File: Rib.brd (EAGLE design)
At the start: 127 x 87.6 mm, 34 parts, among them IC1 REG1117, IC2 REG1117

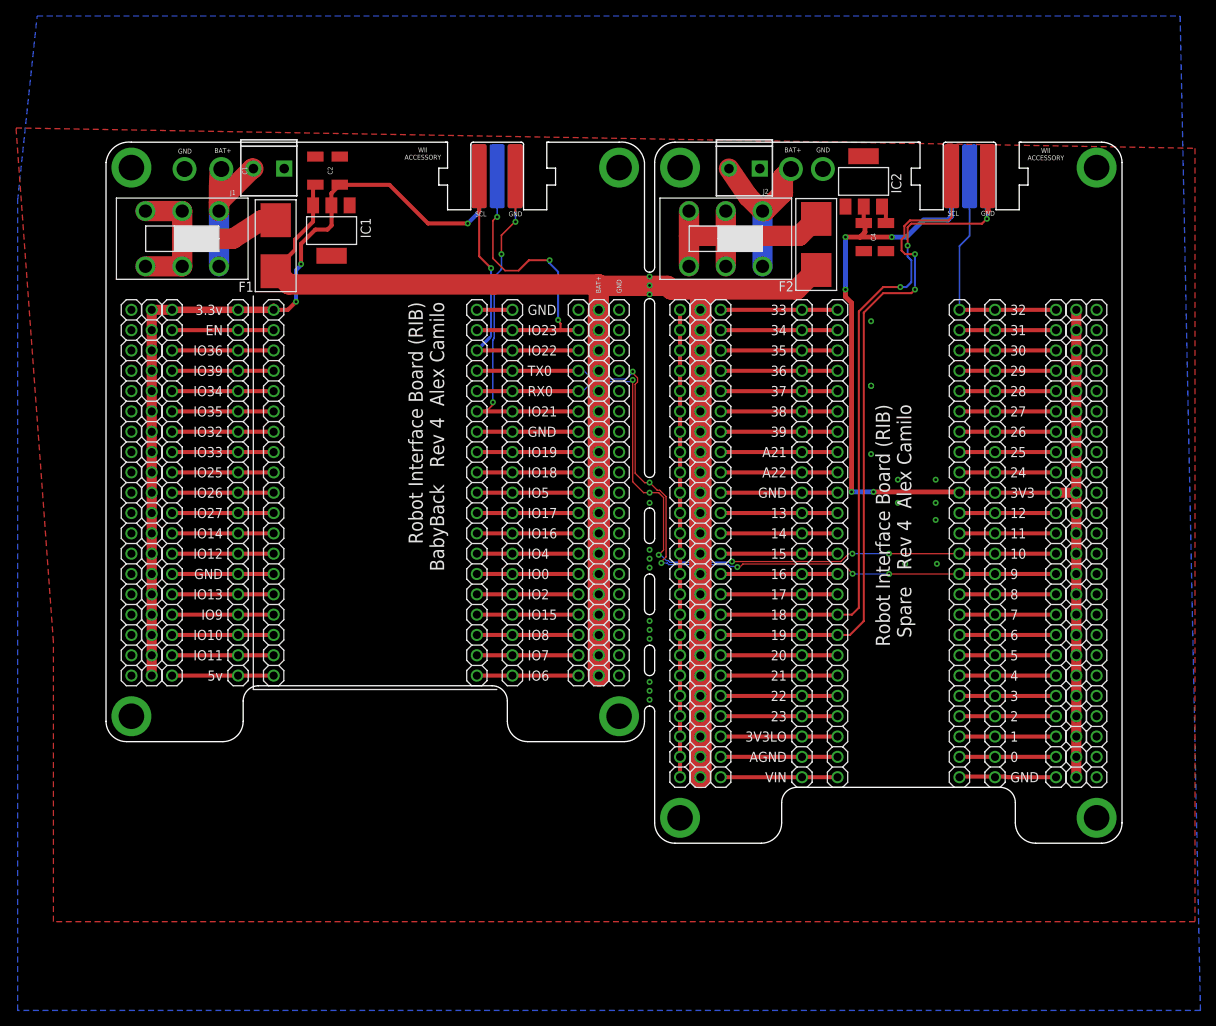
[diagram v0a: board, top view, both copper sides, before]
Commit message: Replaced fuseholder with blade style automotive fuse
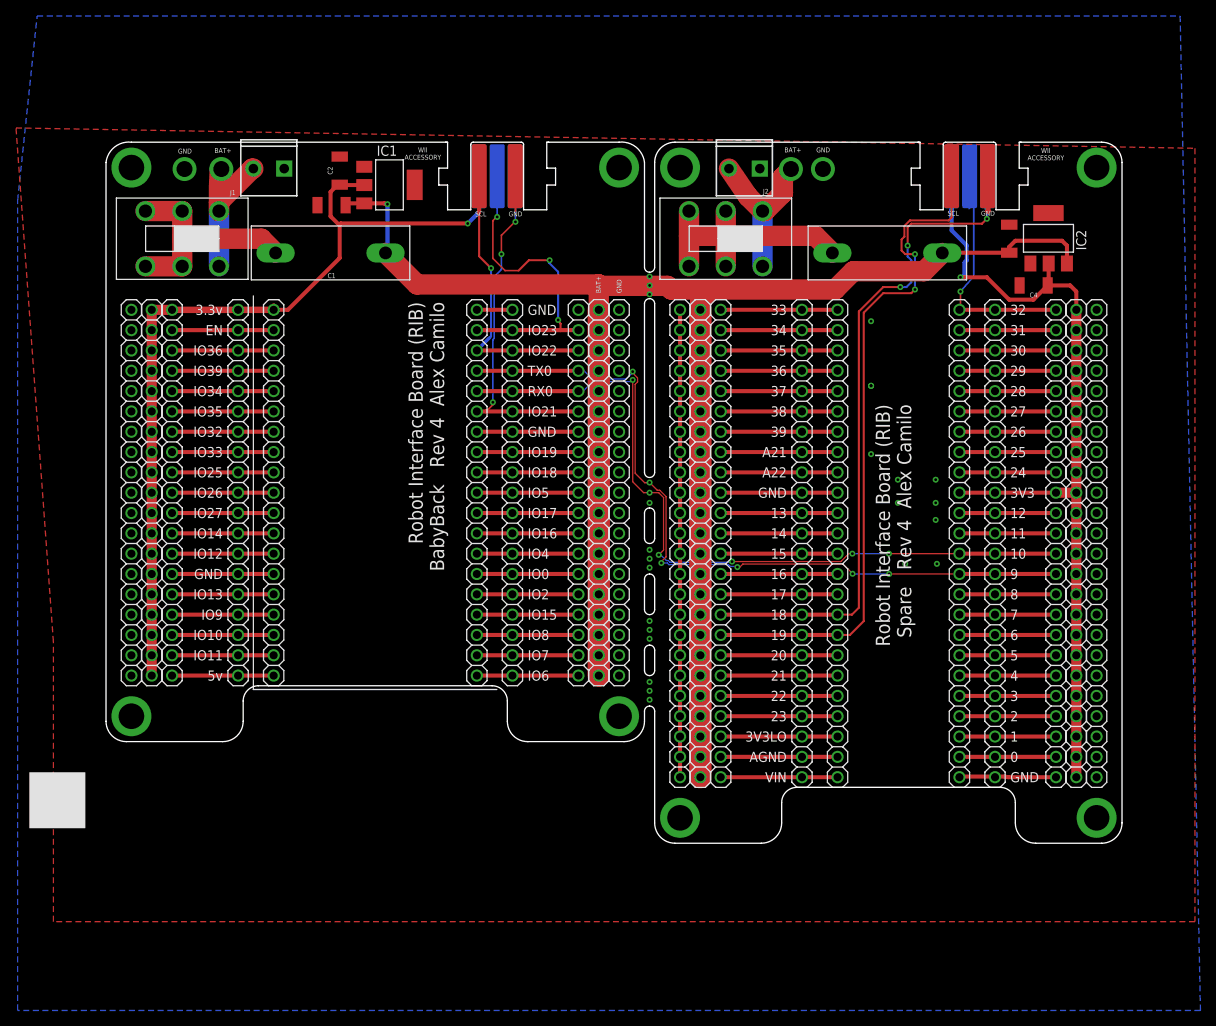
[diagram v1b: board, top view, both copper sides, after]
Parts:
- removed F1, F2: 0154, SMT_Fuse_0154001:0154
- added F3, F4: 3557-2, 3557-2:3557-2
- moved IC2 24.2 mm to (99.4, 59.7)
- moved C4 22.1 mm to (97.5, 53.8), turned to 180 degrees
- moved C3 15.4 mm to (94.5, 59.7), turned to 90 degrees
- moved IC1 9.22 mm to (17.0, 66.4), turned to 270 degrees
- moved C1 4.77 mm to (9.78, 63.9), turned to 180 degrees
- renumbered U$1 to SW1, U$2 to SW2
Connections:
- net LIPORAW: now also F3.P$2, F4.P$2; no longer F1.2, F2.2
- net VCC: now also F3.P$1, F4.P$1; no longer F1.1, F2.1
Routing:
- net V3.3: track 249.3 -> 217.4 mm, vias 8 -> 2
- net VCC: track 242.9 -> 261.9 mm, vias 3 -> 4
- net LIPORAW: track 59.2 -> 61.1 mm
- net DET: track 62.5 -> 64.2 mm, vias 3 -> 4

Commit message: Added Power, Fuse, Regulated satus LEDs
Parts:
- added LED1, LED2, LED3, LED4, LED5, LED6: (no value), eagle-ltspice:LED_SML0603
- added R1, R2, R3, R4, R5, R6: (no value), resistor:R0603
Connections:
- new net N$24: LED1.A, R1.1
- new net N$37: LED2.A, R2.1
- new net N$38: LED3.A, R3.1
- new net N$40: LED4.A, R4.1
- new net N$41: LED5.A, R5.1
- new net N$42: LED6.A, R6.1
- net GND: now also LED1.C, LED2.C, LED3.C, LED4.C, LED5.C, LED6.C
- net LIPORAW: now also R2.2, R5.2
- net V3.3: now also R3.2, R6.2
- net VCC: now also R1.2, R4.2
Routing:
- net VCC: track 261.9 -> 277.4 mm
- net LIPORAW: track 61.1 -> 72.5 mm
- net V3.3: track 217.4 -> 223.6 mm
- net N$41: track 0.00 -> 1.70 mm
- net N$40: track 0.00 -> 1.70 mm
- net N$42: track 0.00 -> 1.70 mm
- net N$24: track 0.00 -> 1.45 mm
- net N$37: track 0.00 -> 1.45 mm
- net N$38: track 0.00 -> 1.45 mm
- net GND: vias 31 -> 33
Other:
- board text added: "3.3v Power"
- board text added: "Battery Power"
- board text added: "Fused VCC"
